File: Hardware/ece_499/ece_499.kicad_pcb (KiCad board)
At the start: 2 copper layers, 110.8 x 70 mm, 60 parts, among them J1 Conn_01x04, J2 Conn_01x04, J3 Conn_01x04, J4 Conn_01x04, J5 Conn_01x04, Q1 DMN2004WK, Q2 DMN2004WK, Q3 DMN2004WK, Q4 DMN2004WK, SW1 Encoder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

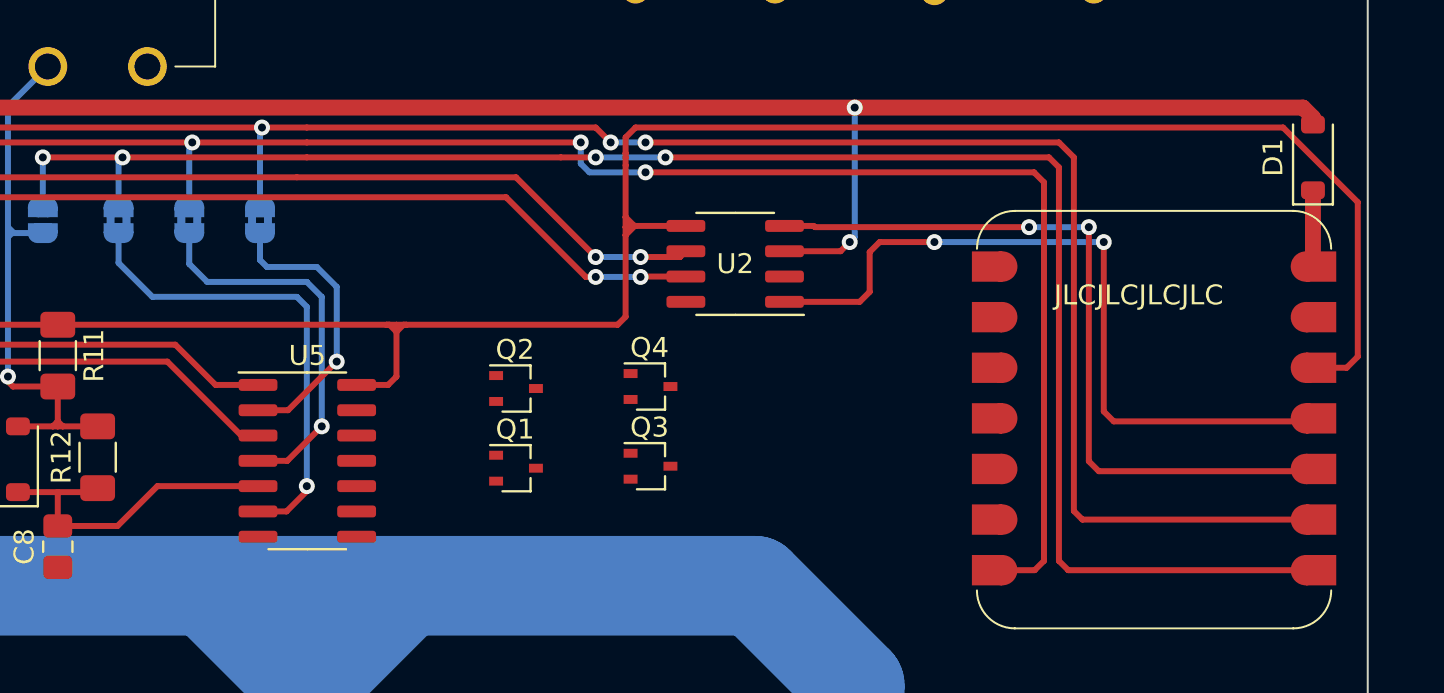
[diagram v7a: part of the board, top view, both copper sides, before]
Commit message: clean up encoder traces
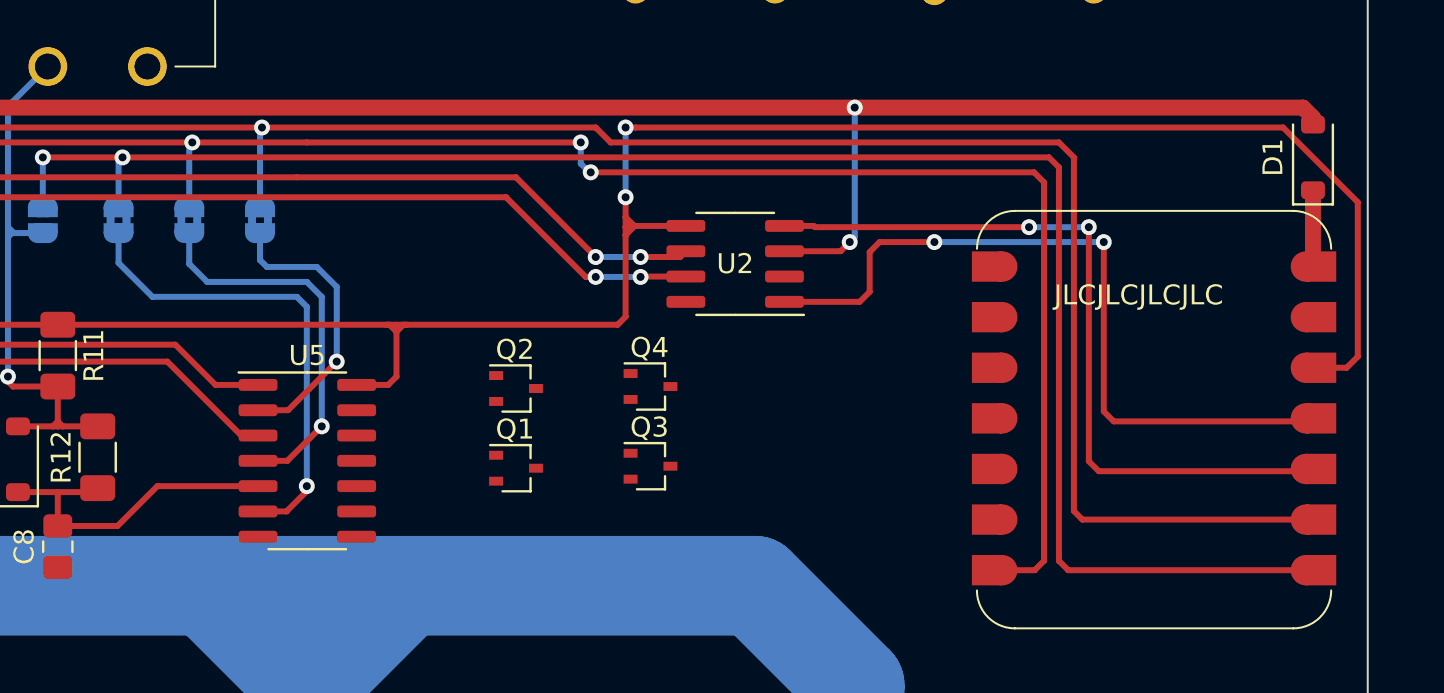
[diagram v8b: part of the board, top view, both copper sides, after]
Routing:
- net +3V3: track 113.5 -> 113.8 mm, vias 0 -> 2
- net controller_sw: vias 4 -> 2
- net controller_B: vias 4 -> 2
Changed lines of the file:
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@@
 	)
 	(segment
-		(start 173.5 56.5)
-		(end 173.5 53.9)
+		(start 174 52)
+		(end 173.5 52)
 		(width 0.3)
 		(layer "F.Cu")
@@
 	)
 	(segment
-		(start 173.5 52.5)
-		(end 173.5 53.3)
+		(start 173.5 56.5)
+		(end 173.5 55.5)
 		(width 0.3)
 		(layer "F.Cu")
@@
 	)
 	(segment
-		(start 174 52)
-		(end 173.5 52.5)
-		(width 0.3)
-		(layer "F.Cu")
-		(net 27)
-	)
-	(segment
 		(start 162 62.25)
 		(end 162 61.9)
@@
 	)
 	(segment
-		(start 173.5 53.5)
-		(end 173.5 53.3)
-		(width 0.3)
-		(layer "F.Cu")
-		(net 27)
-	)
-	(segment
 		(start 176.525 56.94)
 		(end 174 56.94)
@@
 	)
 	(segment
-		(start 173.5 53.9)
-		(end 173.5 53.5)
-		(width 0.3)
-		(layer "F.Cu")
-		(net 27)
-	)
-	(segment
 		(start 162.35 61.9)
 		(end 162 62.25)
@@
 	)
 	(segment
-		(start 173.5 53.3)
-		(end 173.505 53.3)
-		(width 0.3)
-		(layer "F.Cu")
-		(net 27)
-	)
-	(segment
 		(start 162 64.5)
 		(end 162 62.25)
@@
 		(net 27)
 	)
+	(via
+		(at 173.5 52)
+		(size 0.8)
+		(drill 0.4)
+		(layers "F.Cu" "B.Cu")
+		(net 27)
+	)
+	(via
+		(at 173.5 55.5)
+		(size 0.8)
+		(drill 0.4)
+		(layers "F.Cu" "B.Cu")
+		(net 27)
+	)
+	(segment
+		(start 173.5 52)
+		(end 173.5 55.5)
+		(width 0.3)
+		(layer "B.Cu")
+		(net 27)
+	)
 	(segment
 		(start 197.5 66.25)
@@
 	(segment
 		(start 195.25 54)
-		(end 194.75 53.5)
+		(end 195.25 73.75)
 		(width 0.3)
 		(layer "F.Cu")
@@
 	)
 	(segment
-		(start 208.407 74.2185)
+		(start 195.7185 74.2185)
+		(end 208.407 74.2185)
+		(width 0.3)
+		(layer "F.Cu")
+		(net 38)
+	)
+	(segment
+		(start 195.25 73.75)
 		(end 195.7185 74.2185)
 		(width 0.3)
@@
 	)
 	(segment
-		(start 157.5 53.5)
-		(end 170.25 53.5)
+		(start 194.75 53.5)
+		(end 195.25 54)
 		(width 0.3)
 		(layer "F.Cu")
@@
 	(segment
 		(start 148.25 53.5)
-		(end 157.5 53.5)
+		(end 194.75 53.5)
 		(width 0.3)
 		(layer "F.Cu")
 		(net 38)
 	)
-	(segment
-		(start 195.7185 74.2185)
-		(end 195.25 73.75)
-		(width 0.3)
-		(layer "F.Cu")
+	(via
+		(at 148.25 53.5)
+		(size 0.8)
+		(drill 0.4)
+		(layers "F.Cu" "B.Cu")
 		(net 38)
 	)
-	(segment
-		(start 170.25 53.5)
-		(end 172 53.5)
-		(width 0.3)
-		(layer "F.Cu")
-		(net 38)
-	)
-	(segment
-		(start 194.75 53.5)
-		(end 175.5 53.5)
-		(width 0.3)
-		(layer "F.Cu")
-		(net 38)
-	)
-	(segment
-		(start 195.25 73.75)
-		(end 195.25 54)
-		(width 0.3)
-		(layer "F.Cu")
-		(net 38)
-	)
-	(via
-		(at 172 53.5)
-		(size 0.8)
-		(drill 0.4)
-		(layers "F.Cu" "B.Cu")
-		(net 38)
-	)
-	(via
-		(at 148.25 53.5)
-		(size 0.8)
-		(drill 0.4)
-		(layers "F.Cu" "B.Cu")
-		(net 38)
-	)
-	(via
-		(at 175.5 53.5)
-		(size 0.8)
-		(drill 0.4)
-		(layers "F.Cu" "B.Cu")
-		(net 38)
-	)
 	(via
 		(at 144.25 53.5)
@@
 		(drill 0.4)
 		(layers "F.Cu" "B.Cu")
-		(net 38)
-	)
-	(segment
-		(start 172 53.5)
-		(end 175.5 53.5)
-		(width 0.3)
-		(layer "B.Cu")
 		(net 38)
 	)
@@
 	)
 	(segment
+		(start 194.5 54.75)
+		(end 194.5 73.75)
+		(width 0.3)
+		(layer "F.Cu")
+		(net 39)
+	)
+	(segment
+		(start 194 54.25)
+		(end 194.5 54.75)
+		(width 0.3)
+		(layer "F.Cu")
+		(net 39)
+	)
+	(segment
+		(start 194.5 73.75)
+		(end 194.0315 74.2185)
+		(width 0.3)
+		(layer "F.Cu")
+		(net 39)
+	)
+	(segment
 		(start 157.5 52.75)
 		(end 171.25 52.75)
@@
 	)
 	(segment
-		(start 194.5 54.75)
-		(end 194.5 73.75)
-		(width 0.3)
-		(layer "F.Cu")
-		(net 39)
-	)
-	(segment
 		(start 151.75 52.75)
 		(end 157.5 52.75)
@@
 	)
 	(segment
-		(start 174.5 54.25)
-		(end 194 54.25)
-		(width 0.3)
-		(layer "F.Cu")
-		(net 39)
-	)
-	(segment
-		(start 194.5 73.75)
-		(end 194.0315 74.2185)
-		(width 0.3)
-		(layer "F.Cu")
-		(net 39)
-	)
-	(segment
-		(start 194.5 54.75)
+		(start 171.75 54.25)
 		(end 194 54.25)
 		(width 0.3)
@@
 	)
 	(via
+		(at 151.75 52.75)
+		(size 0.8)
+		(drill 0.4)
+		(layers "F.Cu" "B.Cu")
+		(net 39)
+	)
+	(via
+		(at 140.5 52.75)
+		(size 0.8)
+		(drill 0.4)
+		(layers "F.Cu" "B.Cu")
+		(net 39)
+	)
+	(via
+		(at 171.75 54.25)
+		(size 0.8)
+		(drill 0.4)
+		(layers "F.Cu" "B.Cu")
+		(net 39)
+	)
+	(via
 		(at 171.25 52.75)
-		(size 0.8)
-		(drill 0.4)
-		(layers "F.Cu" "B.Cu")
-		(net 39)
-	)
-	(via
-		(at 151.75 52.75)
-		(size 0.8)
-		(drill 0.4)
-		(layers "F.Cu" "B.Cu")
-		(net 39)
-	)
-	(via
-		(at 140.5 52.75)
-		(size 0.8)
-		(drill 0.4)
-		(layers "F.Cu" "B.Cu")
-		(net 39)
-	)
-	(via
-		(at 174.5 54.25)
 		(size 0.8)
 		(drill 0.4)
@@
 	)
 	(segment
-		(start 174.5 54.25)
-		(end 171.689339 54.25)
+		(start 171.689339 54.25)
+		(end 171.75 54.25)
 		(width 0.3)
 		(layer "B.Cu")
@@
 	)
 	(segment
+		(start 196.4285 71.6785)
+		(end 208.407 71.6785)
+		(width 0.3)
+		(layer "F.Cu")
+		(net 40)
+	)
+	(segment
 		(start 155.25 52)
-		(end 157.5 52)
+		(end 172 52)
 		(width 0.3)
 		(layer "F.Cu")
@@
 	)
 	(segment
-		(start 157.5 52)
-		(end 172 52)
+		(start 195.25 52.75)
+		(end 196 53.5)
 		(width 0.3)
 		(layer "F.Cu")
@@
 	)
 	(segment
-		(start 196 71.25)
-		(end 196 53.5)
+		(start 172.75 52.75)
+		(end 195.25 52.75)
 		(width 0.3)
 		(layer "F.Cu")
@@
 	)
 	(segment
-		(start 208.407 71.6785)
-		(end 196.4285 71.6785)
+		(start 196 53.5)
+		(end 196 71.25)
 		(width 0.3)
 		(layer "F.Cu")
@@
 	)
 	(segment
-		(start 195.25 52.75)
-		(end 174.5 52.75)
-		(width 0.3)
-		(layer "F.Cu")
-		(net 40)
-	)
-	(segment
-		(start 196 53.5)
-		(end 195.25 52.75)
-		(width 0.3)
-		(layer "F.Cu")
-		(net 40)
-	)
-	(segment
-		(start 196.4285 71.6785)
-		(end 196 71.25)
+		(start 196 71.25)
+		(end 196.4285 71.6785)
 		(width 0.3)
 		(layer "F.Cu")
@@
 	)
 	(via
-		(at 172.75 52.75)
-		(size 0.8)
-		(drill 0.4)
-		(layers "F.Cu" "B.Cu")
-		(net 40)
-	)
-	(via
 		(at 137 52)
-		(size 0.8)
-		(drill 0.4)
-		(layers "F.Cu" "B.Cu")
-		(net 40)
-	)
-	(via
-		(at 174.5 52.75)
 		(size 0.8)
 		(drill 0.4)
@@
 		(width 0.3)
 		(layer "B.Cu")
-		(net 40)
-	)
-	(segment
-		(start 172.75 52.75)
-		(end 174.5 52.75)
-		(width 0.3)
-		(layer "B.Cu")
